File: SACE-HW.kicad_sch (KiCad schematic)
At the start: 4 parts

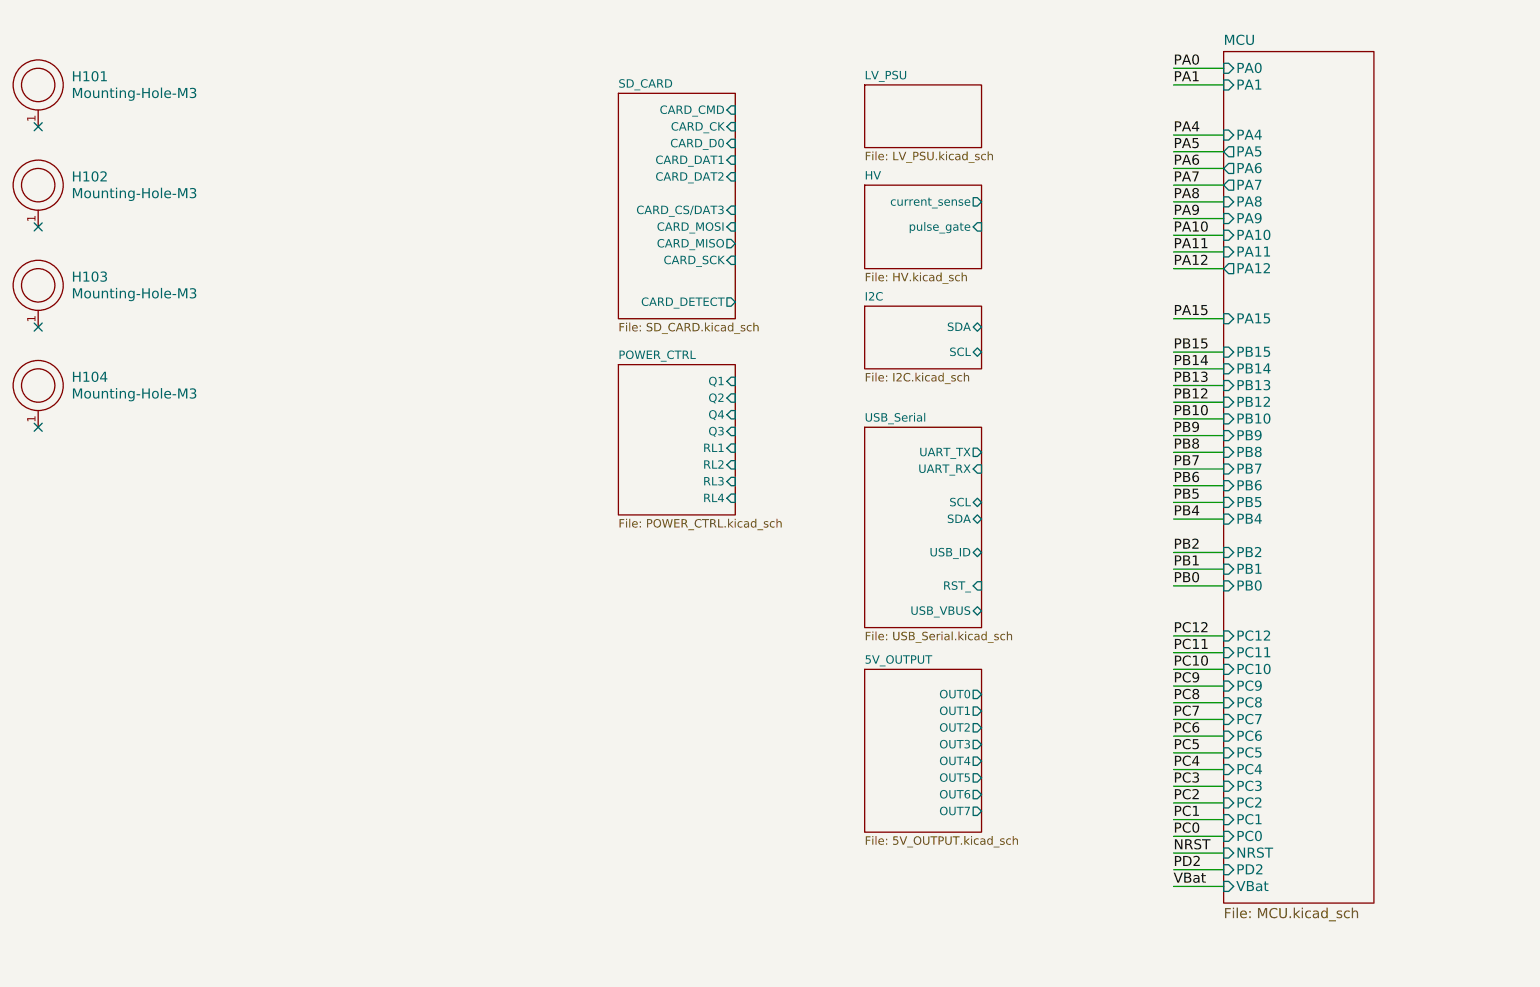
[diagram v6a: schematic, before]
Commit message: update schematic
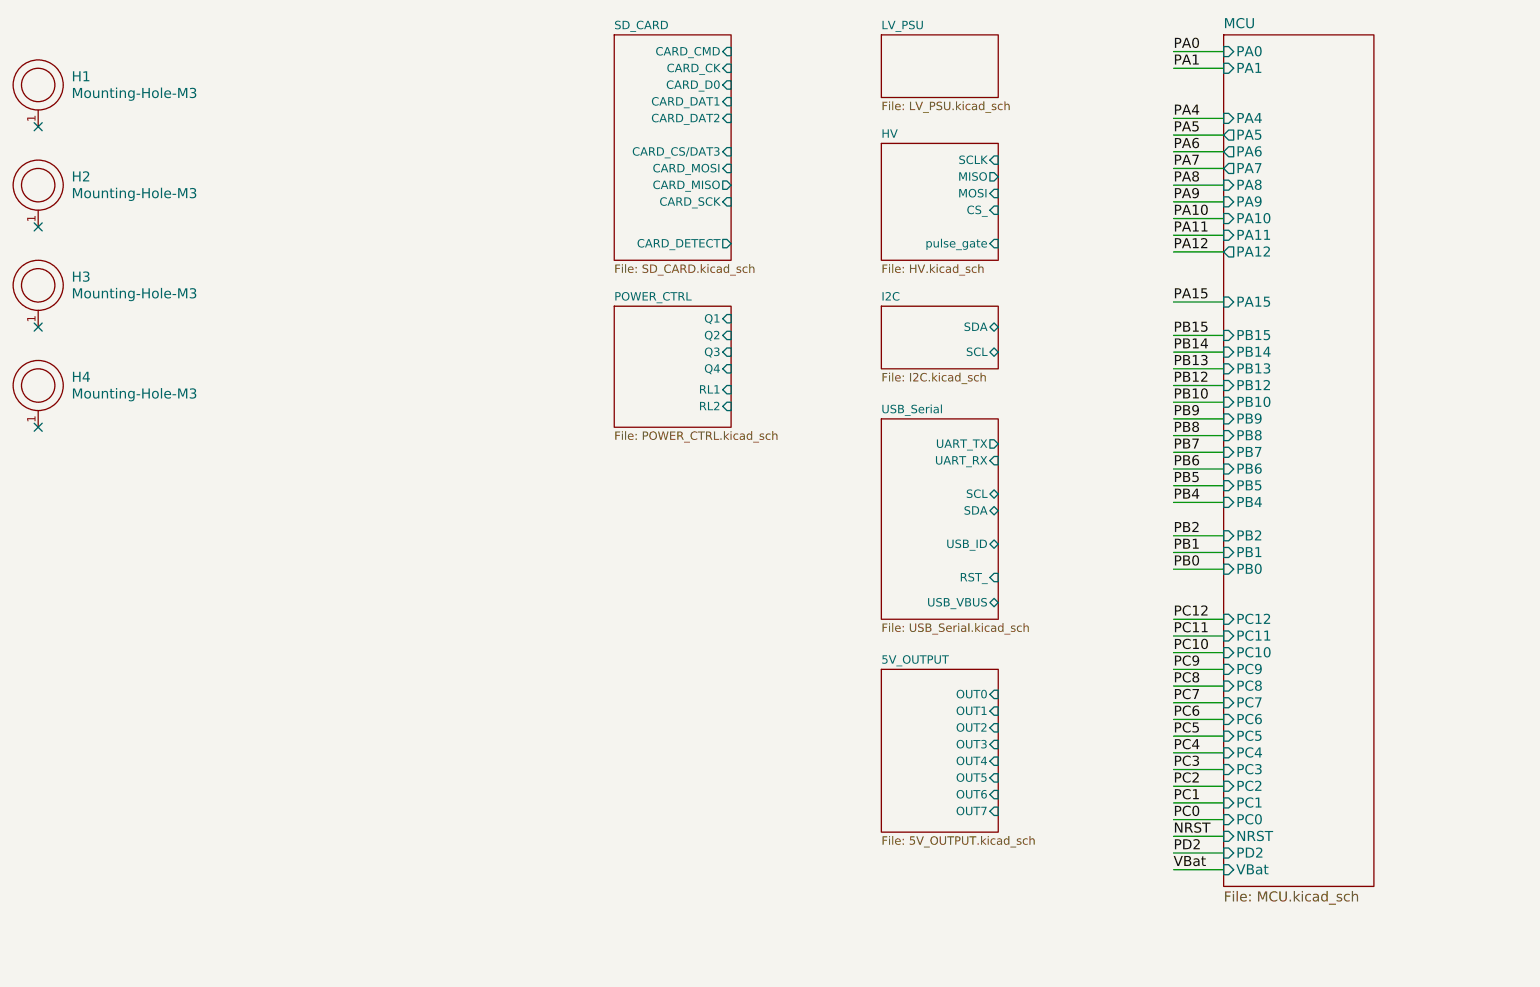
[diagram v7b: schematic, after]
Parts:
- renumbered H101 to H1, H102 to H2, H103 to H3, H104 to H4
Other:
- sheet HV ports: added CS_, MISO, MOSI, SCLK; removed current_sense
- sheet POWER_CTRL ports: added none; removed RL3, RL4

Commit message: finalisation de la schématique
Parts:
- added C101: 885012207098, Capacitors:C0805, symbol Capacitors:885012207098
- added J101: Header_Male_Pin_2.54mm_1X5_,_Unshrouded, Connectors:Headers_2.54mm_1X5, symbol Connectors:Header_Male_Pin_2.54mm_1X5_,_Unshrouded
- added R101: RC0805JR-074K7L, Resistors:R0805, symbol Resistors:RC0805JR-074K7L
- added R102: RC0805JR-07150RL, Resistors:R0805, symbol Resistors:RC0805JR-07150RL
- renumbered H1 to H101, H2 to H102, H3 to H103, H4 to H104
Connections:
- net PA0: now also J101.4
- net PA1: now also J101.3
- net PA15: now also C101.1, R102.2
- new net: J101.5, R101.1, R102.1
- new net GNDB: C101.2, J101.1
- new net VDD: J101.2, R101.2
- no-connect marks 4 -> 8
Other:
- sheet MCU ports: added USART2_RX, USART2_TX; removed none
- sheet USB_Serial ports: added none; removed USB_ID
